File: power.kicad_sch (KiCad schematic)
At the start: 20 parts, among them J1 USB_C_Receptacle_USB2.0_16P, J6 JST-SM02B-SRSS-TB, Q1 Si2301CDS, SW62 MSK-12C02, U2 USBLC6-2SC6, U3 TP4056, U4 XC6206PxxxMR

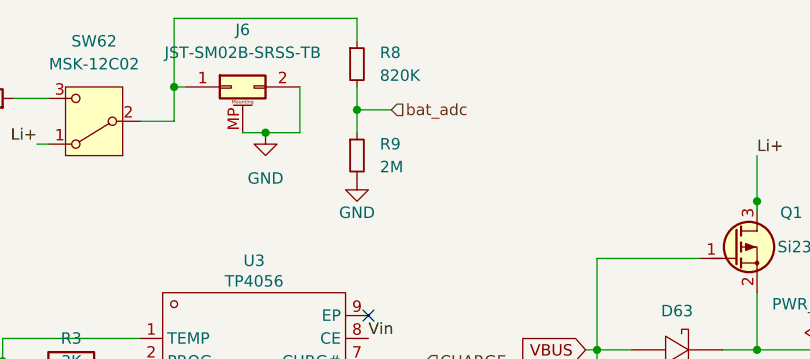
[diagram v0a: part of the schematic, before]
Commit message: feat: update pcb, use xc6206, optimize routing
Signed-off-by: HaoboGu <haobogu@outlook.com>
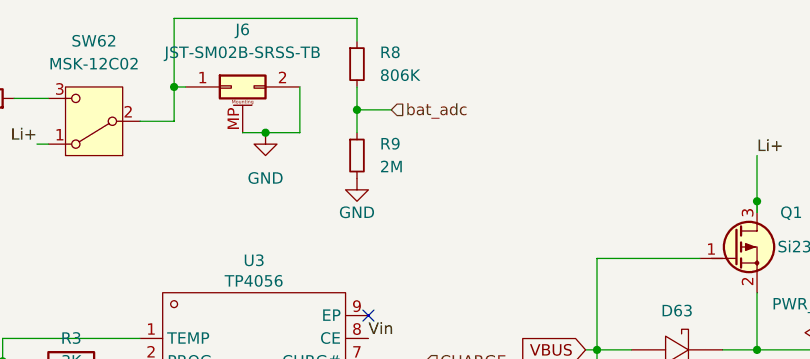
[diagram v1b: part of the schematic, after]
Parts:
- R8: value 820K -> 806K
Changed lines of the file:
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@@
 			)
 		)
-		(property "Value" "820K"
+		(property "Value" "806K"
 			(at 199.39 35.5599 0)
 			(effects

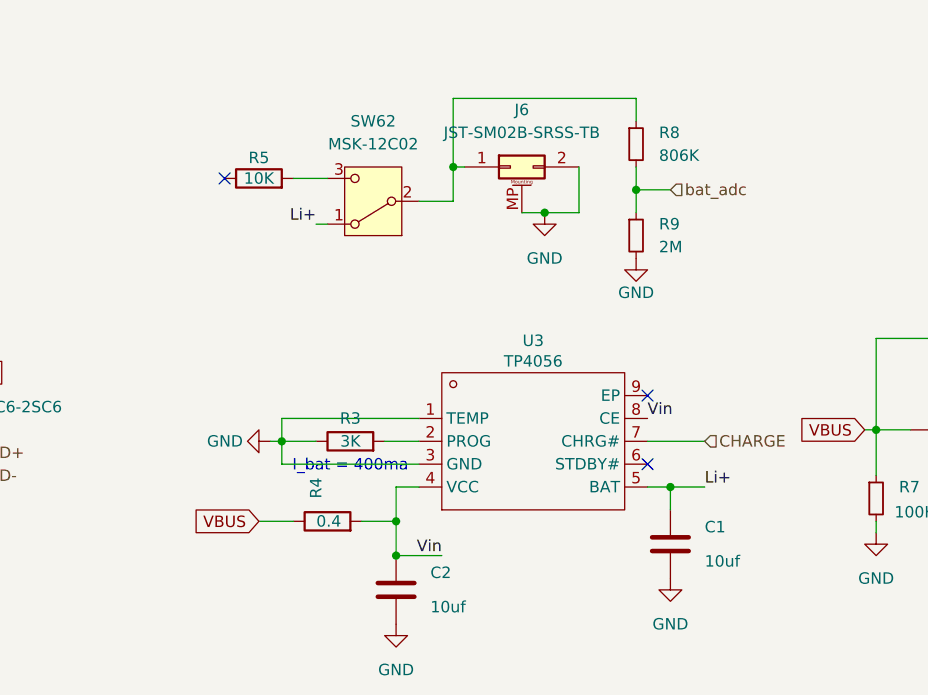
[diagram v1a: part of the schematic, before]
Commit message: update battery socket
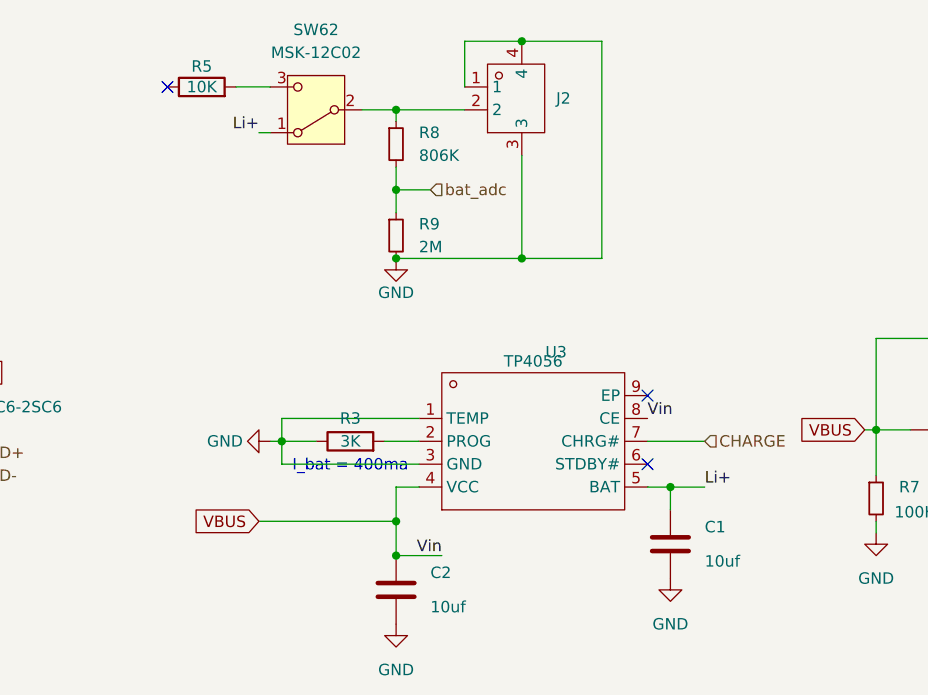
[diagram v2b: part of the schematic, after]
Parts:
- removed J6: JST-SM02B-SRSS-TB, Connector_JST:JST_SH_SM02B-SRSS-TB_1x02-1MP_P1.00mm_Horizontal, symbol Connector_Generic_MountingPin:Conn_02x01_MountingPin
- removed R4: 0.4, Resistor_SMD:R_0805_2012Metric_Pad1.20x1.40mm_HandSolder, symbol Device:R
- added J2: ~, XY-MX1.25-2A71:CONN-SMD_2P-P1.25_XYECONN_XY-MX1.25-2A71, symbol XY-MX1.25-2A71:XY-MX1.25-2A71
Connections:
- net Vin is gone; now on net VBUS: C2.1, U3.4 (VCC), U3.8 (CE)
- net GND: now also J2.1, J2.3, J2.4
- net at R8.1, SW62.2 (B): now also J2.2
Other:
- moved on the sheet: R5, R8, R9, SW62
